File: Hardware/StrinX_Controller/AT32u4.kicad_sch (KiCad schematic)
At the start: 16 parts, among them J1 HWB, SW1 RST, U1 ATmega32U4-A, Y1 16MHz

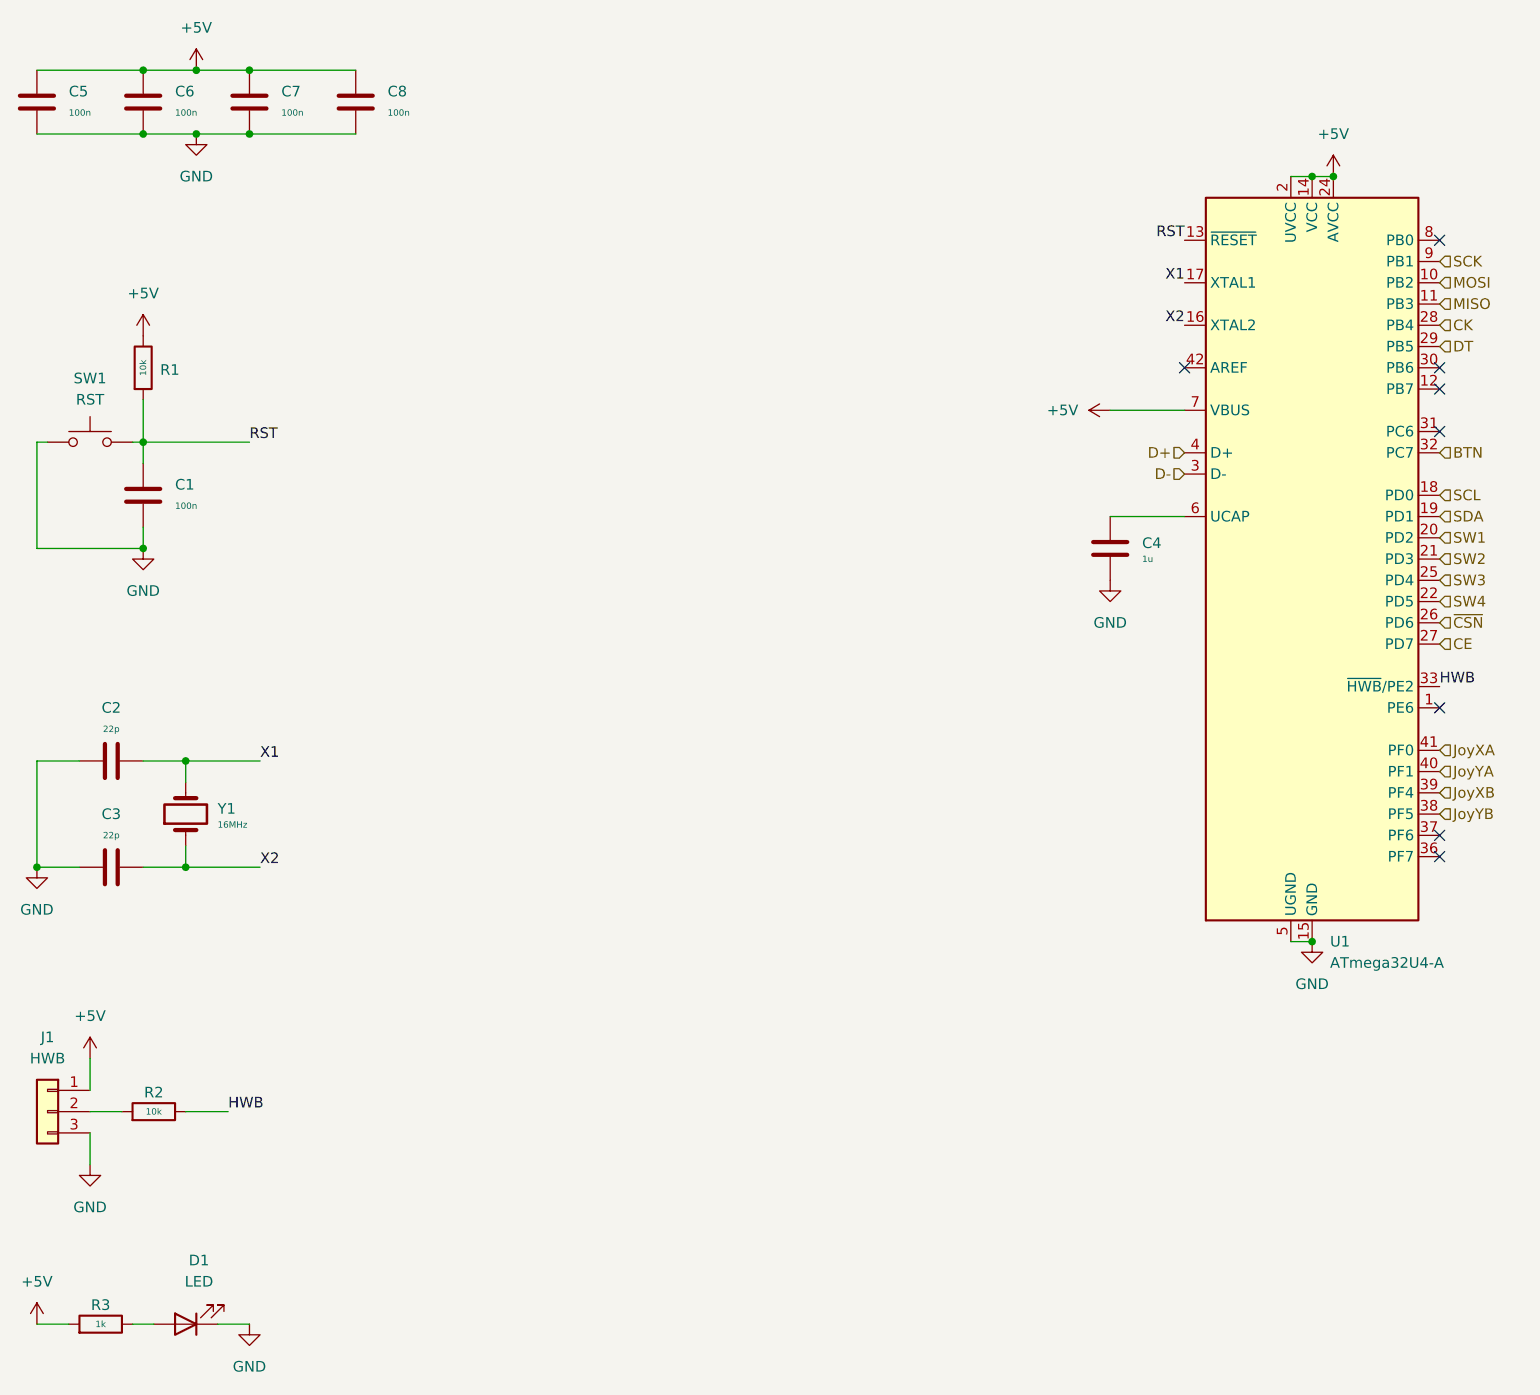
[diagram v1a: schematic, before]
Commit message: Add device and footprint
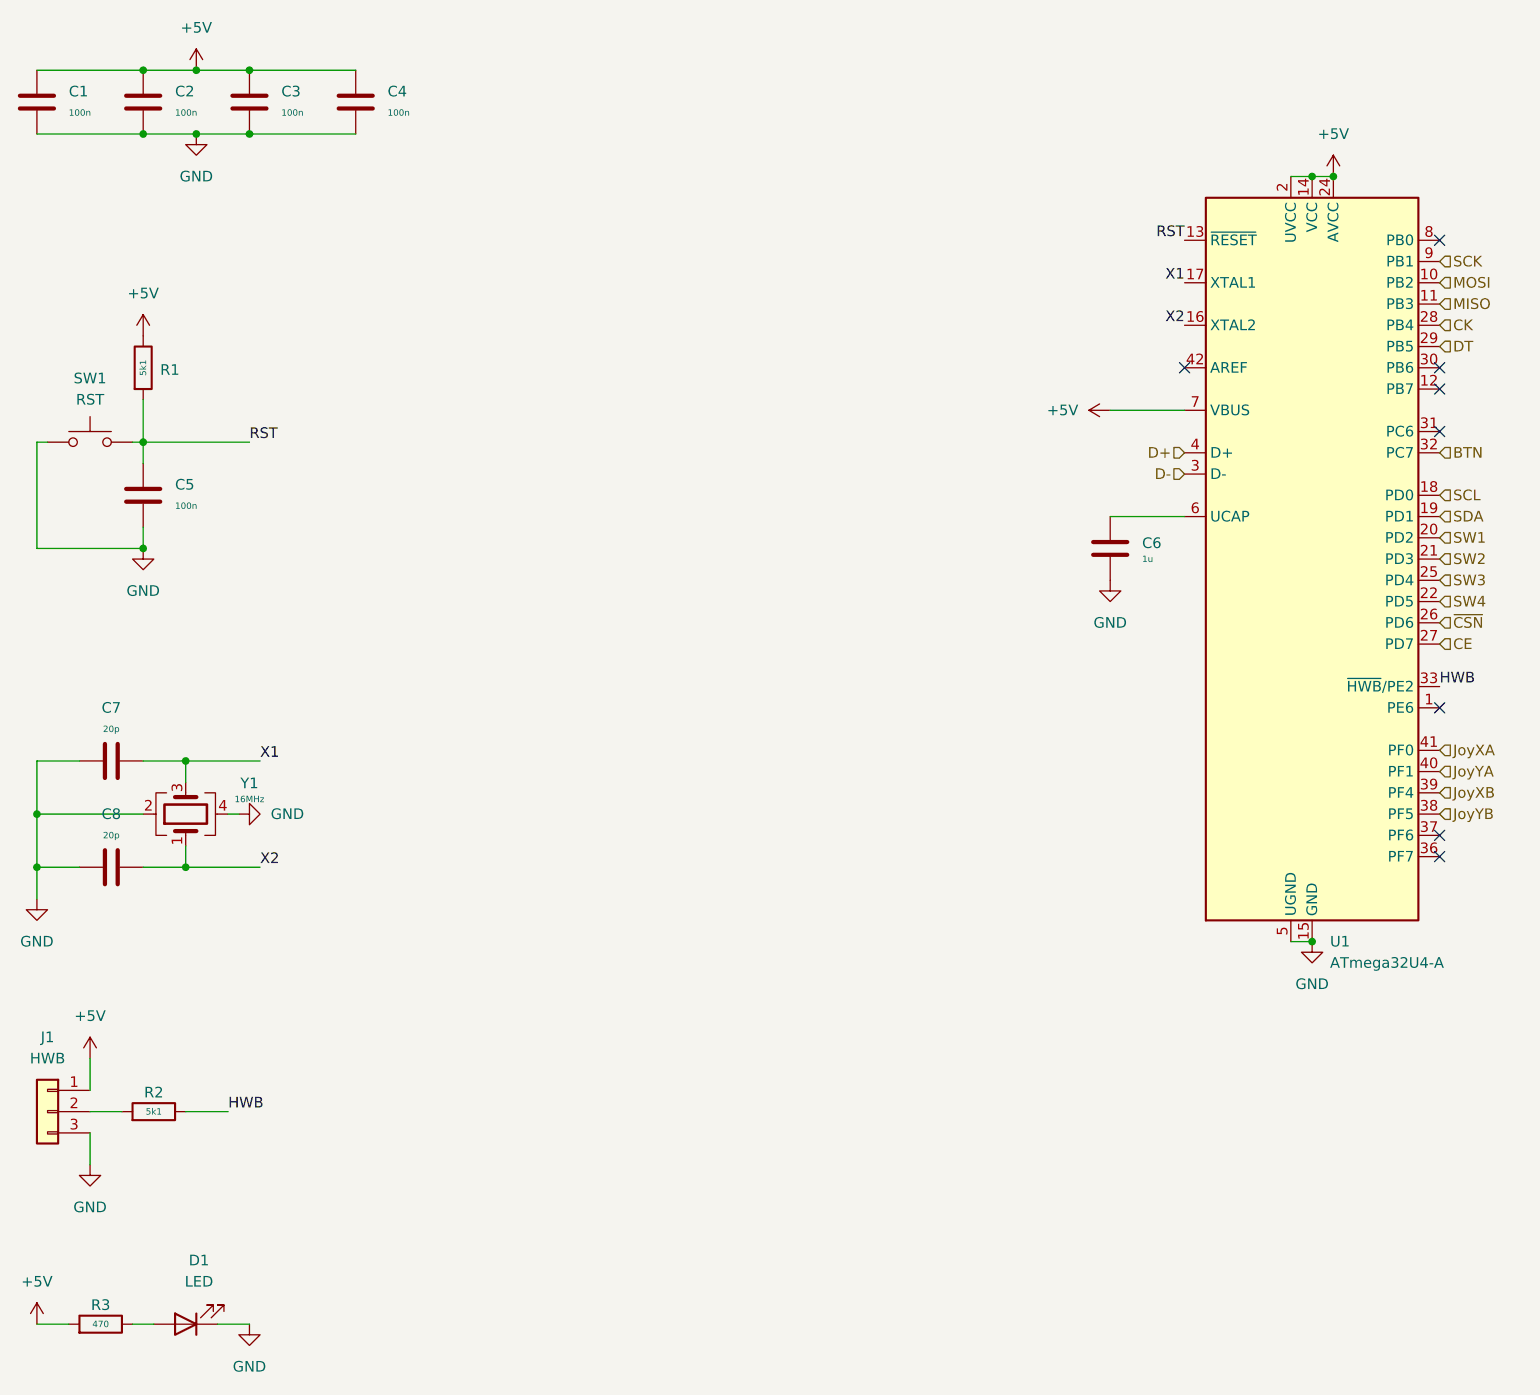
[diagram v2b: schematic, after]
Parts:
- removed Y1: 16MHz, symbol Device:Crystal
- added Y1: 16MHz, Crystal:Crystal_SMD_7050-4Pin_7.0x5.0mm, symbol Device:Crystal_GND24
- C1: renamed from C5; footprint (none) -> Capacitor_SMD:C_0603_1608Metric
- C2: renamed from C6; footprint (none) -> Capacitor_SMD:C_0603_1608Metric
- C3: renamed from C7; footprint (none) -> Capacitor_SMD:C_0603_1608Metric
- C4: renamed from C8; footprint (none) -> Capacitor_SMD:C_0603_1608Metric
- C5: renamed from C1; footprint (none) -> Capacitor_SMD:C_0603_1608Metric
- C6: renamed from C4; footprint (none) -> Capacitor_SMD:C_0603_1608Metric
- C7: renamed from C2; value 22p -> 20p; footprint (none) -> Capacitor_SMD:C_0603_1608Metric
- C8: renamed from C3; value 22p -> 20p; footprint (none) -> Capacitor_SMD:C_0603_1608Metric
- D1: footprint (none) -> LED_SMD:LED_1206_3216Metric
- J1: footprint (none) -> Connector_PinHeader_2.54mm:PinHeader_1x03_P2.54mm_Vertical
- R1, R2: value 10k -> 5k1; footprint (none) -> Resistor_SMD:R_0603_1608Metric
- R3: value 1k -> 470; footprint (none) -> Resistor_SMD:R_0603_1608Metric
- SW1: footprint (none) -> Button_Switch_THT:SW_PUSH_6mm_H4.3mm
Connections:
- net GND: now also Y1.2, Y1.4
- net X1: now also Y1.3
- net X2: now also Y1.1

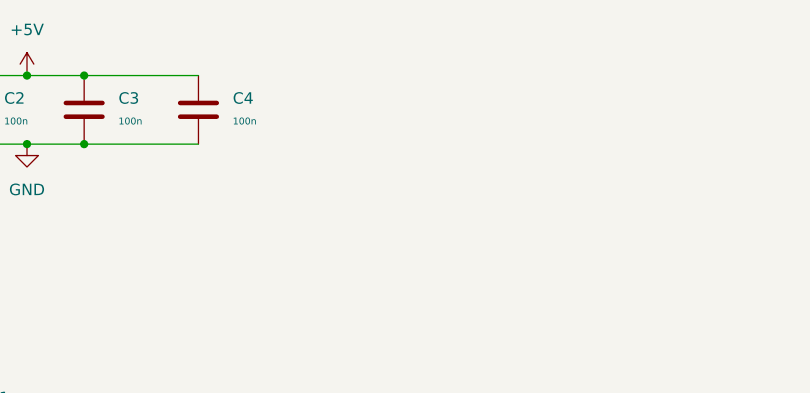
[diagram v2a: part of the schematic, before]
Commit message: Add some capacitor for MCU
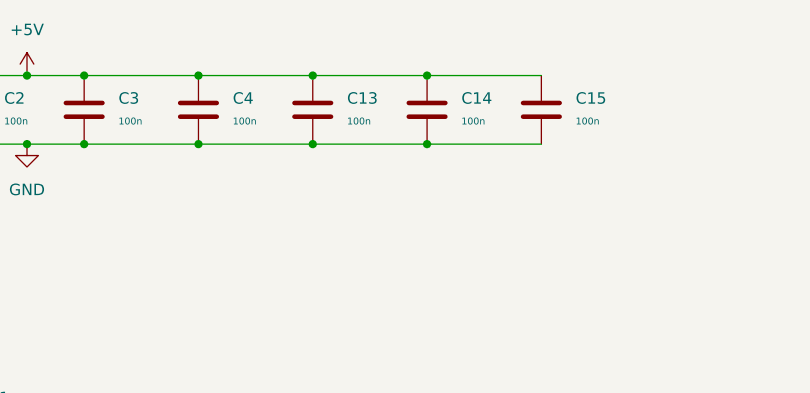
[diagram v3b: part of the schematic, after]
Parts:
- added C13, C14, C15: 100n, Capacitor_SMD:C_0603_1608Metric, symbol Device:C
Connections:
- net +5V: now also C13.1, C14.1, C15.1
- net GND: now also C13.2, C14.2, C15.2
